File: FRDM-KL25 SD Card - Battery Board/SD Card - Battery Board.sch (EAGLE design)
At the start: 63 parts, among them J3 SSW-108-02-S-D, J4 SSW-110-02-S-D, J5 SSW-108-02-S-D, J6 SSW-106-02-S-D, U1 TPS63001, U2 TPS63002, U3 BQ27510DRZT-G3, U4 BQ24210DQCT

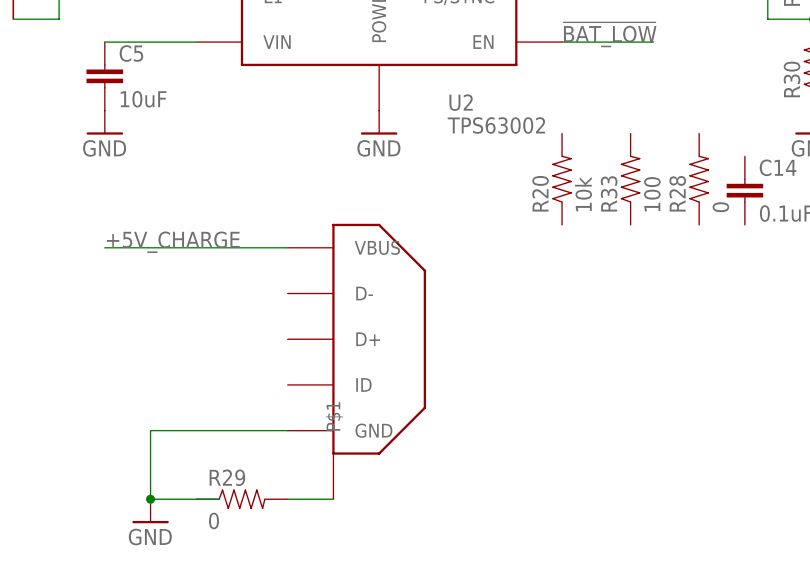
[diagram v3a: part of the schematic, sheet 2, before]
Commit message: FRDM-KL25Z Changed 0603 components to 0402 where possible
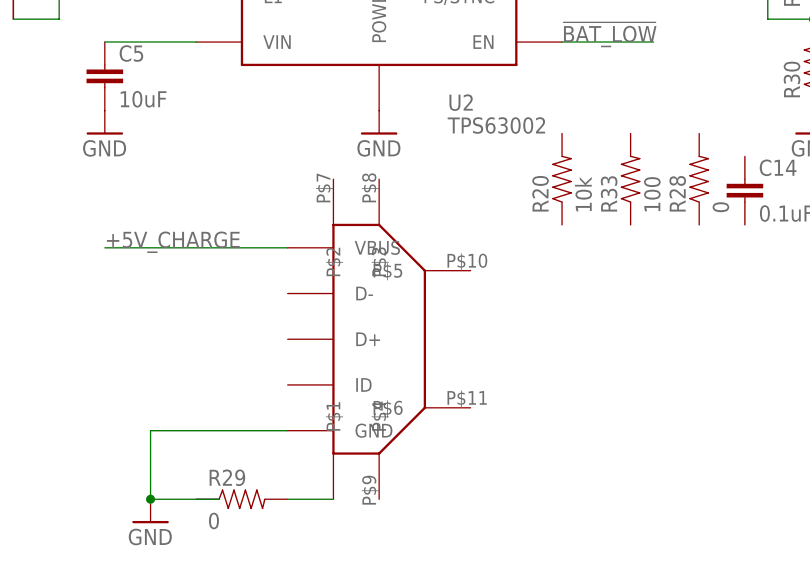
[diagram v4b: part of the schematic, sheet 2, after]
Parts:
- C10, C11, C12: device Kas-Capacitors:CAPACITOR0.1U-X5R-10%25V-0603 -> Kas-Capacitors:CAPACITOR0.1-X5R-10%-16V-0402
- C13, C14: device Kas-Capacitors:CAPACITOR0.1U-X7R-10%-25V-0603 -> Kas-Capacitors:CAPACITOR0.1U-X7R-10%-25V
- C6: device Kas-Capacitors:CAPACITOR10U-X7R-10%-25 -> Kas-Capacitors:CAPACITOR10U-X7R-10%-6.3V
- R14, R26: device Kas-Resistors:RESISTOR1K-62.5M-0.1%-75V -> Kas-Resistors:RESISTOR0-100M-X%-50V
- R15, R16, R32, R33: device Kas-Resistors:RESISTOR100-62.5M-0.1%-75V -> Kas-Resistors:RESISTOR100-63M-1%50V-0402
- R22: device Kas-Resistors:RESISTOR1.6K-125M-0.1%-100V -> Kas-Resistors:RESISTOR1.6K-63M-1%-50V-0402
- R23: device Kas-Resistors:RESISTOR20K-63M-1%-50V -> Kas-Resistors:RESISTOR0-100M-X%-50V
- R30, R31: device Kas-Resistors:RESISTOR0603 -> Kas-Resistors:RESISTOR0402
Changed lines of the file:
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@@
 <part name="R13" library="Kas-Resistors" deviceset="RESISTOR" device="10K-62.5M-1%-50V" value="10k"/>
 <part name="D2" library="Kas-Diodes-LEDs" deviceset="1.6X3.2" device="R-1.85V-20MA" value="Red-LED"/>
-<part name="R14" library="Kas-Resistors" deviceset="RESISTOR" device="1K-62.5M-0.1%-75V" value="1k"/>
+<part name="R14" library="Kas-Resistors" deviceset="RESISTOR" device="0-100M-X%-50V" value="1k"/>
 <part name="GND2" library="supply1" deviceset="GND" device=""/>
-<part name="R15" library="Kas-Resistors" deviceset="RESISTOR" device="100-62.5M-0.1%-75V" value="100"/>
+<part name="R15" library="Kas-Resistors" deviceset="RESISTOR" device="100-63M-1%50V-0402" value="100"/>
 <part name="GND3" library="supply1" deviceset="GND" device=""/>
-<part name="R16" library="Kas-Resistors" deviceset="RESISTOR" device="100-62.5M-0.1%-75V" value="100"/>
+<part name="R16" library="Kas-Resistors" deviceset="RESISTOR" device="100-63M-1%50V-0402" value="100"/>
 <part name="R17" library="Kas-Resistors" deviceset="RESISTOR" device="0.01-100M-1%-50V" value="0.01"/>
 <part name="R18" library="Kas-Resistors" deviceset="RESISTOR" device="10K-62.5M-1%-50V" value="10k"/>
@@
 <part name="R20" library="Kas-Resistors" deviceset="RESISTOR" device="10K-62.5M-1%-50V" value="10k"/>
 <part name="R21" library="Kas-Resistors" deviceset="RESISTOR" device="10K-62.5M-1%-50V" value="10k"/>
-<part name="R22" library="Kas-Resistors" deviceset="RESISTOR" device="1.6K-125M-0.1%-100V" value="1.6k"/>
-<part name="R23" library="Kas-Resistors" deviceset="RESISTOR" device="20K-63M-1%-50V" value="20k"/>
+<part name="R22" library="Kas-Resistors" deviceset="RESISTOR" device="1.6K-63M-1%-50V-0402" value="1.6k"/>
+<part name="R23" library="Kas-Resistors" deviceset="RESISTOR" device="0-100M-X%-50V" value="20k"/>
 <part name="R24" library="Kas-Resistors" deviceset="RESISTOR" device="10K-62.5M-1%-50V" value="10k"/>
 <part name="R25" library="Kas-Resistors" deviceset="RESISTOR" device="10K-62.5M-1%-50V" value="10k"/>
-<part name="R26" library="Kas-Resistors" deviceset="RESISTOR" device="1K-62.5M-0.1%-75V" value="1k"/>
+<part name="R26" library="Kas-Resistors" deviceset="RESISTOR" device="0-100M-X%-50V" value="1k"/>
 <part name="D1" library="Kas-Diodes-LEDs" deviceset="1.6X3.2" device="Y-X.XX-XXMA" value="Yellow-LED"/>
 <part name="J1" library="Kas-Connectors" deviceset="SD_CARD_SLOT" device=""/>
@@
 <part name="C4" library="Kas-Capacitors" deviceset="CAPACITOR" device="10U-X7R-10%-6.3V" value="10uF"/>
 <part name="C5" library="Kas-Capacitors" deviceset="CAPACITOR" device="10U-X7R-10%-6.3V" value="10uF"/>
-<part name="C6" library="Kas-Capacitors" deviceset="CAPACITOR" device="10U-X7R-10%-25" value="10uF"/>
+<part name="C6" library="Kas-Capacitors" deviceset="CAPACITOR" device="10U-X7R-10%-6.3V" value="10uF"/>
 <part name="C7" library="Kas-Capacitors" deviceset="CAPACITOR" device="0.1U-X7R-10%-25V" value="0.1uF"/>
 <part name="C8" library="Kas-Capacitors" deviceset="CAPACITOR" device="1U-X5R-10%-10V-0603" value="1uF"/>
 <part name="C1" library="Kas-Capacitors" deviceset="CAPACITOR" device="0.47U-X5R-10%-10V-0603" value="0.47uF"/>
 <part name="C9" library="Kas-Capacitors" deviceset="CAPACITOR" device="0.47U-X5R-10%-10V-0603" value="0.47uF"/>
-<part name="C10" library="Kas-Capacitors" deviceset="CAPACITOR" device="0.1U-X5R-10%25V-0603" value="0.1uF"/>
-<part name="C11" library="Kas-Capacitors" deviceset="CAPACITOR" device="0.1U-X5R-10%25V-0603" value="0.1uF"/>
-<part name="C12" library="Kas-Capacitors" deviceset="CAPACITOR" device="0.1U-X5R-10%25V-0603" value="0.1uF"/>
+<part name="C10" library="Kas-Capacitors" deviceset="CAPACITOR" device="0.1-X5R-10%-16V-0402" value="0.1uF"/>
+<part name="C11" library="Kas-Capacitors" deviceset="CAPACITOR" device="0.1-X5R-10%-16V-0402" value="0.1uF"/>
+<part name="C12" library="Kas-Capacitors" deviceset="CAPACITOR" device="0.1-X5R-10%-16V-0402" value="0.1uF"/>
 <part name="D3" library="Kas-Diodes-LEDs" deviceset="SCHOTTKY" device=""/>
 <part name="D4" library="Kas-Diodes-LEDs" deviceset="SCHOTTKY" device=""/>
@@
 <part name="R28" library="Kas-Resistors" deviceset="RESISTOR" device="0-100M-X%-50V" value="0"/>
 <part name="R29" library="Kas-Resistors" deviceset="RESISTOR" device="0-100M-X%-50V" value="0"/>
-<part name="R30" library="Kas-Resistors" deviceset="RESISTOR" device="0603" value="DNP"/>
-<part name="R31" library="Kas-Resistors" deviceset="RESISTOR" device="0603" value="DNP"/>
+<part name="R30" library="Kas-Resistors" deviceset="RESISTOR" device="0402" value="DNP"/>
+<part name="R31" library="Kas-Resistors" deviceset="RESISTOR" device="0402" value="DNP"/>
 <part name="L1" library="Kas-Inductors" deviceset="TY0NRS4010T2R2MDGG" device="" value="2.2uH"/>
 <part name="L2" library="Kas-Inductors" deviceset="TY0NRS4010T2R2MDGG" device="" value="2.2uH"/>
-<part name="R32" library="Kas-Resistors" deviceset="RESISTOR" device="100-62.5M-0.1%-75V" value="100"/>
-<part name="R33" library="Kas-Resistors" deviceset="RESISTOR" device="100-62.5M-0.1%-75V" value="100"/>
-<part name="C13" library="Kas-Capacitors" deviceset="CAPACITOR" device="0.1U-X7R-10%-25V-0603" value="0.1uF"/>
-<part name="C14" library="Kas-Capacitors" deviceset="CAPACITOR" device="0.1U-X7R-10%-25V-0603" value="0.1uF"/>
+<part name="R32" library="Kas-Resistors" deviceset="RESISTOR" device="100-63M-1%50V-0402" value="100"/>
+<part name="R33" library="Kas-Resistors" deviceset="RESISTOR" device="100-63M-1%50V-0402" value="100"/>
+<part name="C13" library="Kas-Capacitors" deviceset="CAPACITOR" device="0.1U-X7R-10%-25V" value="0.1uF"/>
+<part name="C14" library="Kas-Capacitors" deviceset="CAPACITOR" device="0.1U-X7R-10%-25V" value="0.1uF"/>
 <part name="GND4" library="Kas-Pwr" deviceset="GND" device=""/>
 <part name="P+1" library="Kas-Pwr" deviceset="VCC" device=""/>

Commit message: FRDM-KL25Z: Changed LEDs to smaller size, added nets with names and considerd other connections to shield b naming nets to connectors
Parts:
- added R34: DNP, Kas-Resistors:RESISTOR0402
- C8: device Kas-Capacitors:CAPACITOR1U-X5R-10%-10V-0603 -> Kas-Capacitors:CAPACITOR1U-X5R-10%-10V
- D1: value Yellow-LED -> Blue-LED; device Kas-Diodes-LEDs:1.6X3.2Y-X.XX-XXMA -> Kas-Diodes-LEDs:0.8X1.2BLUE-3.3V-20M
- D2: value Red-LED -> Green-LED; device Kas-Diodes-LEDs:1.6X3.2R-1.85V-20MA -> Kas-Diodes-LEDs:0.8X1.2GREEN-3.3V-20M
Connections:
- net N$17 renamed SPI-CSB-SD
- net N$18 renamed SPI-MOSI
- net N$20 renamed SD-CARD-DETECT
- net N$21 renamed SD-WRITE-PROTECT
- net N$22 renamed SPI-SCLK
- net N$23 renamed PS/SYNC-2
- net N$24 renamed SPI-MISO
- net N$27 renamed PS/SYNC-1
- new net 3.3V++: J5-3.1, J5-7.1
- new net 5V++: J5-9.1
- new net I2C-SCL-0: J3-4.1
- new net I2C-SCL-1.0: J4-2.1
- new net I2C-SCL-1.1: J3-3.1
- new net I2C-SCL-1.2: J6-11.1
- new net I2C-SDA-0: J3-2.1
- new net I2C-SDA-1.0: J4-4.1
- new net I2C-SDA-1.1: J3-1.1
- new net I2C-SDA-1.2: J6-9.1
- new net INT1-21002: J3-6.1
- new net INT1-8700: J3-12.1
- new net INT2-21002: J4-20.1
- new net INT2-8700: J3-8.1
- new net N$3: R34.1, U4.VDPM
- new net SOI-MISO-0.0: J4-12.1
- new net SPI-CSB-21002: J4-16.1
- new net SPI-CSB-8700: J6-5.1
- new net SPI-MISO-0.1: J3-15.1
- new net SPI-MOSI-0.0: J4-14.1
- new net SPI-MOSI-0.1: J3-5.1
- new net SPI-SCK-0.0: J4-10.1
- new net SPI-SCK-0.1: J3-7.1
- new net VIN: J5-15.1
- net GND: now also J4-8.1, J5-11.1, J5-13.1, R34.2
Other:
- note added: "NEED TO ADD BATTERY CONNECTION"
- note added: "Self EN"
- moved on the sheet: J3-1, J3-10, J3-11, J3-12, J3-13, J3-14, J3-15, J3-16, J3-2, J3-3, J3-4, J3-5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

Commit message: FRDM-KL25Z: Updated components to be correct
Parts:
- C1, C9: device Kas-Capacitors:CAPACITOR0.47U-X5R-10%-10V-0603 -> Kas-Capacitors:CAPACITOR0.47U-X5R-10%-6.3V-0402
- R14, R26: device Kas-Resistors:RESISTOR0-100M-X%-50V -> Kas-Resistors:RESISTOR1K-63M-1%-50V-0402
- R15, R16, R32, R33: device Kas-Resistors:RESISTOR100-63M-1%50V-0402 -> Kas-Resistors:RESISTOR1K-63M-1%-50V-0402
- R23: device Kas-Resistors:RESISTOR0-100M-X%-50V -> Kas-Resistors:RESISTOR20K-63M-1%-50V-0402
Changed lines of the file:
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@@
 <part name="R13" library="Kas-Resistors" deviceset="RESISTOR" device="10K-62.5M-1%-50V" value="10k"/>
 <part name="D2" library="Kas-Diodes-LEDs" deviceset="0.8X1.2" device="GREEN-3.3V-20M" value="Green-LED"/>
-<part name="R14" library="Kas-Resistors" deviceset="RESISTOR" device="0-100M-X%-50V" value="1k"/>
+<part name="R14" library="Kas-Resistors" deviceset="RESISTOR" device="1K-63M-1%-50V-0402" value="1k"/>
 <part name="GND2" library="supply1" deviceset="GND" device=""/>
-<part name="R15" library="Kas-Resistors" deviceset="RESISTOR" device="100-63M-1%50V-0402" value="100"/>
+<part name="R15" library="Kas-Resistors" deviceset="RESISTOR" device="1K-63M-1%-50V-0402" value="100"/>
 <part name="GND3" library="supply1" deviceset="GND" device=""/>
-<part name="R16" library="Kas-Resistors" deviceset="RESISTOR" device="100-63M-1%50V-0402" value="100"/>
+<part name="R16" library="Kas-Resistors" deviceset="RESISTOR" device="1K-63M-1%-50V-0402" value="100"/>
 <part name="R17" library="Kas-Resistors" deviceset="RESISTOR" device="0.01-100M-1%-50V" value="0.01"/>
 <part name="R18" library="Kas-Resistors" deviceset="RESISTOR" device="10K-62.5M-1%-50V" value="10k"/>
@@
 <part name="R21" library="Kas-Resistors" deviceset="RESISTOR" device="10K-62.5M-1%-50V" value="10k"/>
 <part name="R22" library="Kas-Resistors" deviceset="RESISTOR" device="1.6K-63M-1%-50V-0402" value="1.6k"/>
-<part name="R23" library="Kas-Resistors" deviceset="RESISTOR" device="0-100M-X%-50V" value="20k"/>
+<part name="R23" library="Kas-Resistors" deviceset="RESISTOR" device="20K-63M-1%-50V-0402" value="20k"/>
 <part name="R24" library="Kas-Resistors" deviceset="RESISTOR" device="10K-62.5M-1%-50V" value="10k"/>
 <part name="R25" library="Kas-Resistors" deviceset="RESISTOR" device="10K-62.5M-1%-50V" value="10k"/>
-<part name="R26" library="Kas-Resistors" deviceset="RESISTOR" device="0-100M-X%-50V" value="1k"/>
+<part name="R26" library="Kas-Resistors" deviceset="RESISTOR" device="1K-63M-1%-50V-0402" value="1k"/>
 <part name="D1" library="Kas-Diodes-LEDs" deviceset="0.8X1.2" device="BLUE-3.3V-20M" value="Blue-LED"/>
 <part name="J1" library="Kas-Connectors" deviceset="SD_CARD_SLOT" device=""/>
@@
 <part name="C7" library="Kas-Capacitors" deviceset="CAPACITOR" device="0.1U-X7R-10%-25V" value="0.1uF"/>
 <part name="C8" library="Kas-Capacitors" deviceset="CAPACITOR" device="1U-X5R-10%-10V" value="1uF"/>
-<part name="C1" library="Kas-Capacitors" deviceset="CAPACITOR" device="0.47U-X5R-10%-10V-0603" value="0.47uF"/>
-<part name="C9" library="Kas-Capacitors" deviceset="CAPACITOR" device="0.47U-X5R-10%-10V-0603" value="0.47uF"/>
+<part name="C1" library="Kas-Capacitors" deviceset="CAPACITOR" device="0.47U-X5R-10%-6.3V-0402" value="0.47uF"/>
+<part name="C9" library="Kas-Capacitors" deviceset="CAPACITOR" device="0.47U-X5R-10%-6.3V-0402" value="0.47uF"/>
 <part name="C10" library="Kas-Capacitors" deviceset="CAPACITOR" device="0.1-X5R-10%-16V-0402" value="0.1uF"/>
 <part name="C11" library="Kas-Capacitors" deviceset="CAPACITOR" device="0.1-X5R-10%-16V-0402" value="0.1uF"/>
@@
 <part name="L1" library="Kas-Inductors" deviceset="TY0NRS4010T2R2MDGG" device="" value="2.2uH"/>
 <part name="L2" library="Kas-Inductors" deviceset="TY0NRS4010T2R2MDGG" device="" value="2.2uH"/>
-<part name="R32" library="Kas-Resistors" deviceset="RESISTOR" device="100-63M-1%50V-0402" value="100"/>
-<part name="R33" library="Kas-Resistors" deviceset="RESISTOR" device="100-63M-1%50V-0402" value="100"/>
+<part name="R32" library="Kas-Resistors" deviceset="RESISTOR" device="1K-63M-1%-50V-0402" value="100"/>
+<part name="R33" library="Kas-Resistors" deviceset="RESISTOR" device="1K-63M-1%-50V-0402" value="100"/>
 <part name="C13" library="Kas-Capacitors" deviceset="CAPACITOR" device="0.1U-X7R-10%-25V" value="0.1uF"/>
 <part name="C14" library="Kas-Capacitors" deviceset="CAPACITOR" device="0.1U-X7R-10%-25V" value="0.1uF"/>

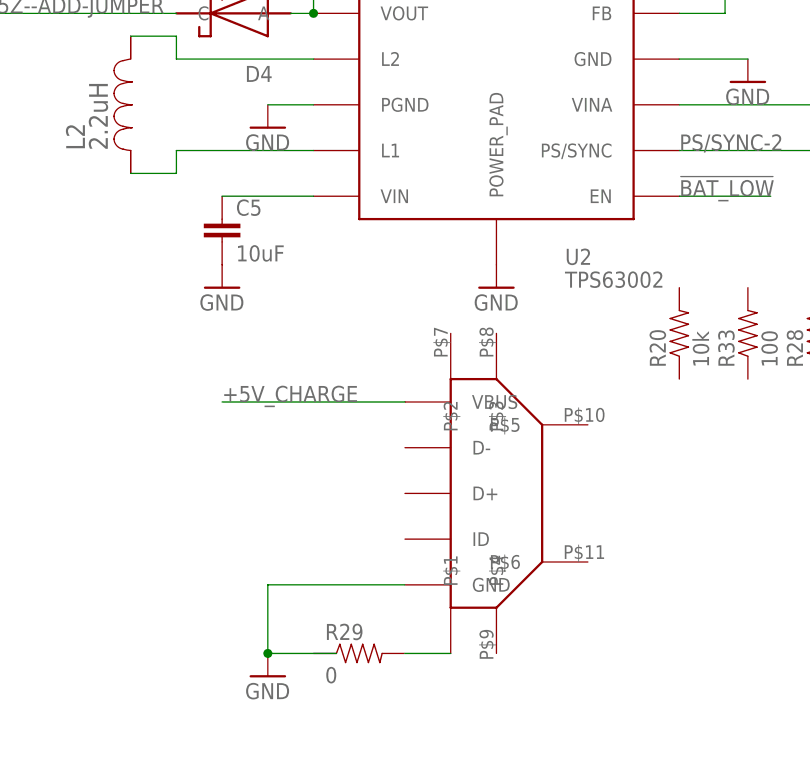
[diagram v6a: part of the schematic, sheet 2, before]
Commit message: FRDM-KL25Z: Grouped and positioned componets now that all are using 0402 corrected packages to be 0402 and rearanged compoinets to better fit space allowed by the PCB
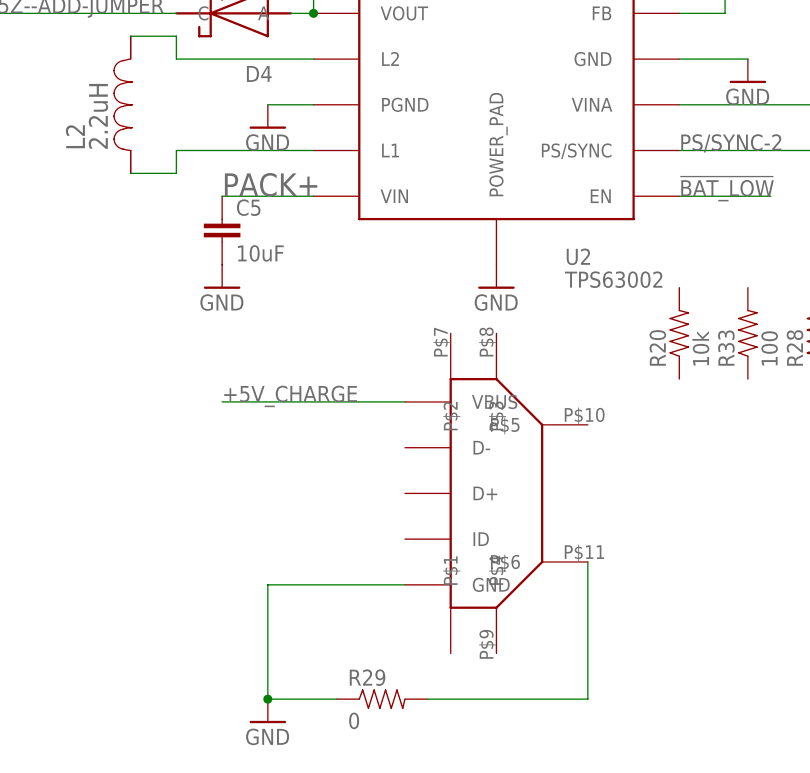
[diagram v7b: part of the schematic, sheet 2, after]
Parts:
- C2, C3, C4, C5, C6: device Kas-Capacitors:CAPACITOR10U-X7R-10%-6.3V -> Kas-Capacitors:CAPACITOR10U-X5R-20%-6.3V-0402
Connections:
- removed net N$12: C5.1, U2.VIN
- net GND: now also R29.1
- net N$28: now also J2.P$6; no longer J2.P$1
- net PACK+: now also C5.1, U2.VIN
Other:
- moved on the sheet: R29
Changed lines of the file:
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@@
 <part name="D1" library="Kas-Diodes-LEDs" deviceset="0.8X1.2" device="BLUE-3.3V-20M" value="Blue-LED"/>
 <part name="J1" library="Kas-Connectors" deviceset="SD_CARD_SLOT" device=""/>
-<part name="C2" library="Kas-Capacitors" deviceset="CAPACITOR" device="10U-X7R-10%-6.3V" value="10uF"/>
-<part name="C3" library="Kas-Capacitors" deviceset="CAPACITOR" device="10U-X7R-10%-6.3V" value="10uF"/>
-<part name="C4" library="Kas-Capacitors" deviceset="CAPACITOR" device="10U-X7R-10%-6.3V" value="10uF"/>
-<part name="C5" library="Kas-Capacitors" deviceset="CAPACITOR" device="10U-X7R-10%-6.3V" value="10uF"/>
-<part name="C6" library="Kas-Capacitors" deviceset="CAPACITOR" device="10U-X7R-10%-6.3V" value="10uF"/>
+<part name="C2" library="Kas-Capacitors" deviceset="CAPACITOR" device="10U-X5R-20%-6.3V-0402" value="10uF"/>
+<part name="C3" library="Kas-Capacitors" deviceset="CAPACITOR" device="10U-X5R-20%-6.3V-0402" value="10uF"/>
+<part name="C4" library="Kas-Capacitors" deviceset="CAPACITOR" device="10U-X5R-20%-6.3V-0402" value="10uF"/>
+<part name="C5" library="Kas-Capacitors" deviceset="CAPACITOR" device="10U-X5R-20%-6.3V-0402" value="10uF"/>
+<part name="C6" library="Kas-Capacitors" deviceset="CAPACITOR" device="10U-X5R-20%-6.3V-0402" value="10uF"/>
 <part name="C7" library="Kas-Capacitors" deviceset="CAPACITOR" device="0.1U-X7R-10%-25V" value="0.1uF"/>
 <part name="C8" library="Kas-Capacitors" deviceset="CAPACITOR" device="1U-X5R-10%-10V" value="1uF"/>
@@
 <instance part="R27" gate="G$1" x="22.86" y="60.96" rot="R90"/>
 <instance part="R28" gate="G$1" x="22.86" y="-10.16" rot="R90"/>
-<instance part="R29" gate="G$1" x="-27.94" y="-45.72"/>
+<instance part="R29" gate="G$1" x="-25.4" y="-50.8"/>
 <instance part="R30" gate="G$1" x="35.56" y="2.54" rot="R90"/>
 <instance part="R31" gate="G$1" x="38.1" y="73.66" rot="R90"/>
@@
 <instance part="GND14" gate="1" x="-43.18" y="-5.08"/>
 <instance part="GND15" gate="1" x="-43.18" y="40.64"/>
-<instance part="GND16" gate="1" x="-38.1" y="-48.26"/>
+<instance part="GND16" gate="1" x="-38.1" y="-53.34"/>
 <instance part="P+3" gate="VCC" x="195.58" y="83.82"/>
 <instance part="P+4" gate="VCC" x="193.04" y="-7.62"/>
@@
 <pinref part="GND16" gate="1" pin="GND"/>
 <wire x1="-22.86" y1="-38.1" x2="-38.1" y2="-38.1" width="0.1524" layer="91"/>
-<wire x1="-38.1" y1="-38.1" x2="-38.1" y2="-45.72" width="0.1524" layer="91"/>
-<wire x1="-30.48" y1="-45.72" x2="-38.1" y2="-45.72" width="0.1524" layer="91"/>
-<junction x="-38.1" y="-45.72"/>
+<wire x1="-38.1" y1="-38.1" x2="-38.1" y2="-50.8" width="0.1524" layer="91"/>
+<wire x1="-30.48" y1="-50.8" x2="-38.1" y2="-50.8" width="0.1524" layer="91"/>
+<junction x="-38.1" y="-50.8"/>
+<pinref part="R29" gate="G$1" pin="1"/>
 </segment>
 <segment>
@@
 <label x="160.02" y="-12.7" size="1.778" layer="95"/>
 </segment>
+<segment>
+<pinref part="U2" gate="G$1" pin="VIN"/>
+<wire x1="-33.02" y1="5.08" x2="-43.18" y2="5.08" width="0.1524" layer="91"/>
+<pinref part="C5" gate="G$1" pin="1"/>
+<label x="-43.18" y="5.08" size="2.54" layer="95" ratio="14"/>
+</segment>
 </net>
 <net name="N$5" class="0">
@@
 </segment>
 </net>
-<net name="N$12" class="0">
-<segment>
-<pinref part="U2" gate="G$1" pin="VIN"/>
-<wire x1="-33.02" y1="5.08" x2="-43.18" y2="5.08" width="0.1524" layer="91"/>
-<pinref part="C5" gate="G$1" pin="1"/>
-</segment>
-</net>
 <net name="N$14" class="0">
 <segment>
@@
 <net name="N$28" class="0">
 <segment>
-<pinref part="J2" gate="G$1" pin="P$1"/>
+<pinref part="J2" gate="G$1" pin="P$6"/>
+<wire x1="-2.54" y1="-35.56" x2="-2.54" y2="-50.8" width="0.1524" layer="91"/>
+<wire x1="-2.54" y1="-50.8" x2="-20.32" y2="-50.8" width="0.1524" layer="91"/>
 <pinref part="R29" gate="G$1" pin="2"/>
-<wire x1="-22.86" y1="-45.72" x2="-17.78" y2="-45.72" width="0.1524" layer="91"/>
-</segment>
-</net>
+</segment>
+</net>
